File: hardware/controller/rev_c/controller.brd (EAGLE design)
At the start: 68.1 x 80 mm, 103 parts, among them J1 DM3AT-SF-PEJM5, J10 SOLDERJUMPERTRACE, J11 SOLDERJUMPERTRACE, J12 SOLDERJUMPERTRACE, J14 TC2030-JLINK-L, J15 TC2030-JLINK-L, J16 U.FL-R-SMT, J2 MICRO_USB_B_HIROSE_ZX62R-B-5P, J3 MICRO_USB_B_HIROSE_ZX62R-B-5P, J4 MODULE_CONTROLLER, J9 SOLDERJUMPERTRACE, Q1 DMN32D2LDF, SW1 B3U-1000P, SW2 PTS810SJ, SW3 SIP3240X, SW4 SIP3240X, SW5 SIP3240X, U1 FM25CLXXB-DG, U2 FTDI234XD, U3 RXM-GPS-RM-T, U4 SAM4LC8BA, U5 SAM4LC8BA, U6 SN74LVC1G125DBVR, U7 TS3USB30E, U8 TXS0108EVQFN20, X1 16MHz, X2 16MHz

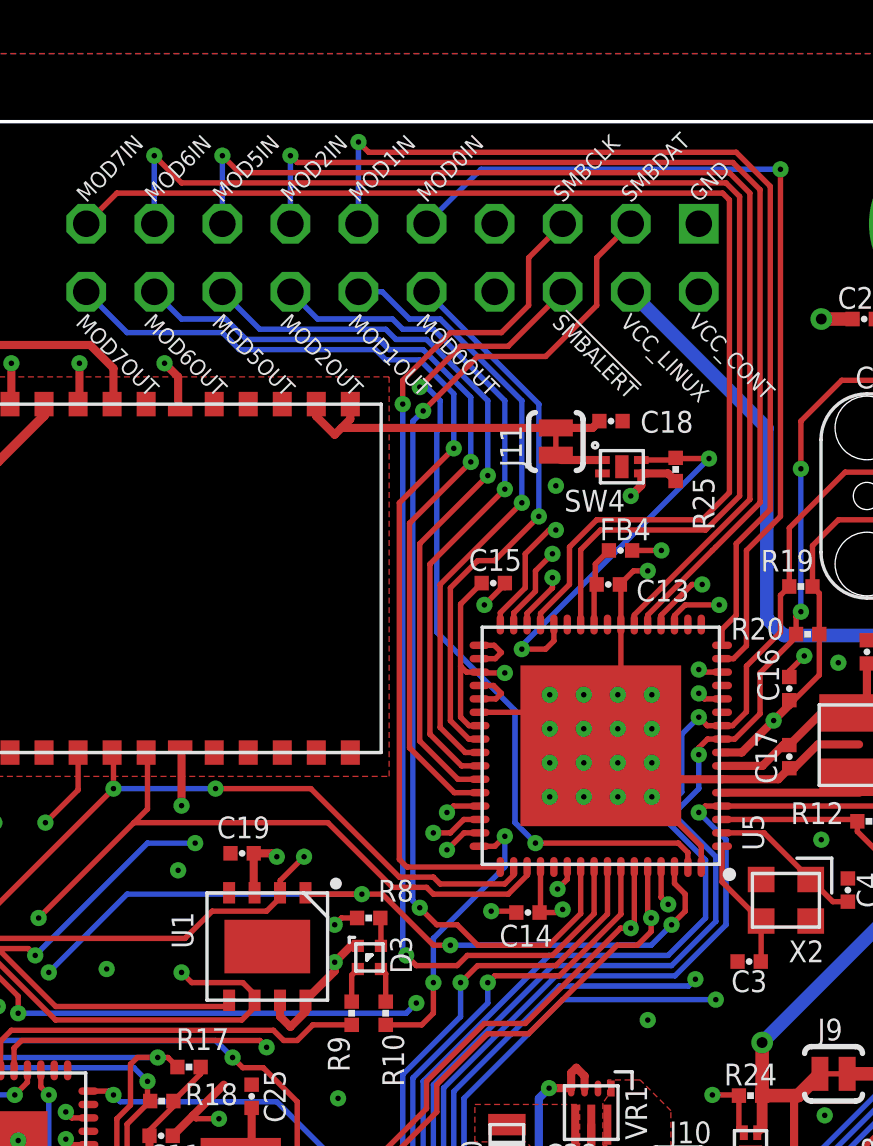
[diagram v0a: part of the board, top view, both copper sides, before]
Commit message: Added watchdog pin
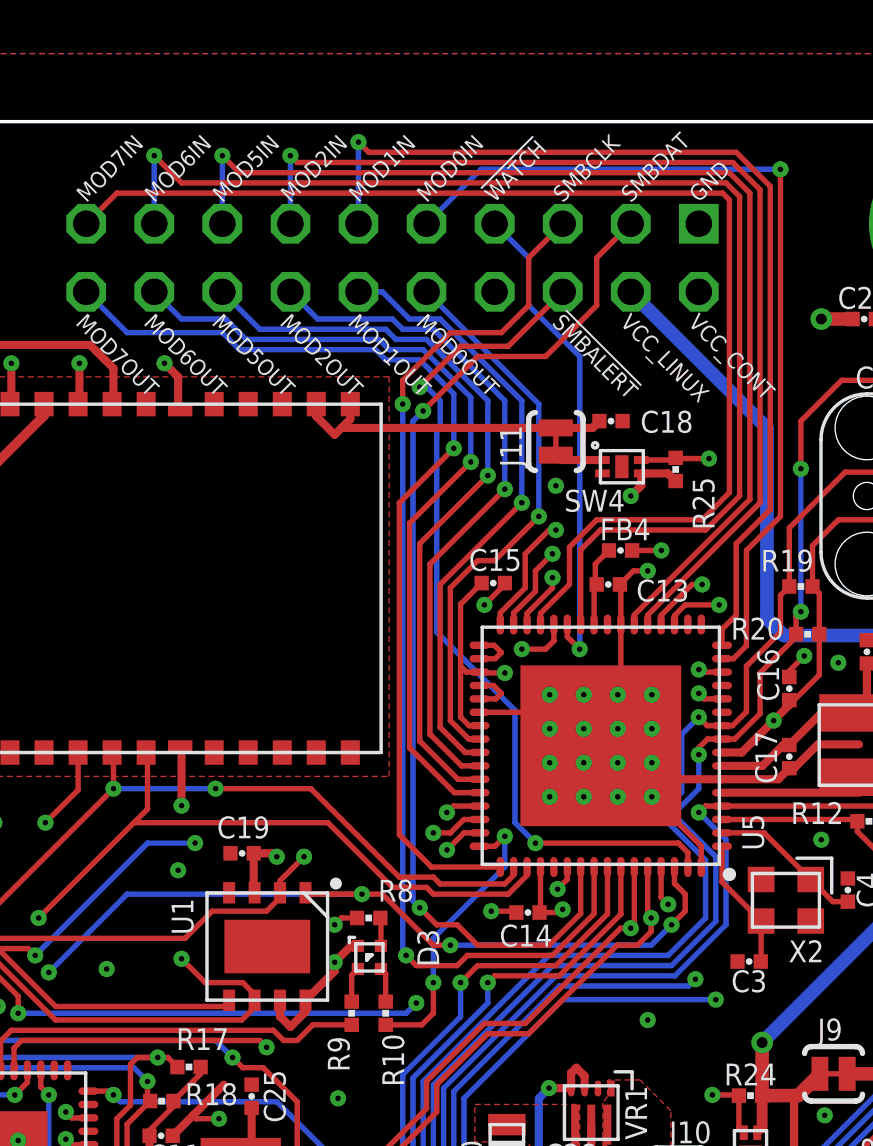
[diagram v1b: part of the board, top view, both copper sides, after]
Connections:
- new net !WATCHDOG: J4.7, U5.27
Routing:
- net !WATCHDOG: track 0.00 -> 18.3 mm, vias 0 -> 1
- net GPS_ENABLE_POWER: track 14.5 -> 15.3 mm
- net MOD7_OUT: track 37.4 -> 36.9 mm
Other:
- board text added: "!WATCH"
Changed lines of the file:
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@@
 <layer number="20" name="Dimension" color="15" fill="1" visible="yes" active="yes"/>
 <layer number="21" name="tPlace" color="7" fill="1" visible="yes" active="yes"/>
-<layer number="22" name="bPlace" color="7" fill="1" visible="yes" active="yes"/>
+<layer number="22" name="bPlace" color="7" fill="1" visible="no" active="yes"/>
 <layer number="23" name="tOrigins" color="15" fill="1" visible="yes" active="yes"/>
-<layer number="24" name="bOrigins" color="15" fill="1" visible="yes" active="yes"/>
+<layer number="24" name="bOrigins" color="15" fill="1" visible="no" active="yes"/>
 <layer number="25" name="tNames" color="7" fill="1" visible="yes" active="yes"/>
-<layer number="26" name="bNames" color="7" fill="1" visible="yes" active="yes"/>
+<layer number="26" name="bNames" color="7" fill="1" visible="no" active="yes"/>
 <layer number="27" name="tValues" color="7" fill="1" visible="no" active="yes"/>
 <layer number="28" name="bValues" color="7" fill="1" visible="no" active="yes"/>
@@
 <text x="27.686" y="-8.382" size="0.6096" layer="21" font="vector" ratio="12" rot="SR90" align="center">Edison
 Program</text>
+<text x="3.81" y="29.972" size="0.6096" layer="21" font="vector" ratio="12" rot="R45">!WATCH</text>
 </plain>
 <attributes>
@@
 <element name="U1" library="chips" package="TDFN-8" value="FM25CLXXB-DG" x="-4.6736" y="2.2352" smashed="yes" rot="R180">
 <attribute name="DIGIKEY" value="FM25CL64B-DGRA-ND" x="-4.6736" y="2.2352" size="1.778" layer="27" rot="R180" display="off"/>
-<attribute name="NAME" x="-8.2442" y="2.8448" size="0.8128" layer="25" font="vector" ratio="12" rot="R270" align="bottom-center"/>
+<attribute name="NAME" x="-8.2442" y="3.3528" size="0.8128" layer="25" font="vector" ratio="12" rot="R270" align="bottom-center"/>
 <attribute name="VALUE" x="-8.0736" y="2.2352" size="1.016" layer="27" font="vector" ratio="12" rot="R270" align="bottom-center"/>
 </element>
@@
 <element name="D3" library="leds" package="1MM_SQ_4PAD" value="SML-LX0404SIUPGUSB" x="-0.8636" y="1.8288" smashed="yes" rot="R90">
 <attribute name="DIGIKEY" value="67-2125-1-ND" x="-0.8636" y="-3.2512" size="1.778" layer="27" rot="R90" display="off"/>
-<attribute name="NAME" x="0.7256" y="1.9304" size="0.8128" layer="25" font="vector" ratio="12" rot="R90" align="bottom-center"/>
+<attribute name="NAME" x="1.7416" y="2.1844" size="0.8128" layer="25" font="vector" ratio="12" rot="R90" align="bottom-center"/>
 <attribute name="VALUE" x="0.9364" y="1.8288" size="1.016" layer="27" font="vector" ratio="12" rot="R90" align="bottom-center"/>
 </element>
@@
 <contactref element="J4" pad="20"/>
 <contactref element="U5" pad="49"/>
-<wire x1="4.0224" y1="5.2032" x2="0.5397" y2="5.2032" width="0.2032" layer="1"/>
-<wire x1="0.5397" y1="5.2032" x2="0.254" y2="5.4889" width="0.2032" layer="1"/>
-<wire x1="0.254" y1="5.4889" x2="0.254" y2="18.796" width="0.2032" layer="1"/>
+<wire x1="4.0224" y1="5.2032" x2="1.45413125" y2="5.2032" width="0.2032" layer="1"/>
+<wire x1="1.45413125" y1="5.2032" x2="0.254" y2="6.40333125" width="0.2032" layer="1"/>
+<wire x1="0.254" y1="6.40333125" x2="0.254" y2="18.796" width="0.2032" layer="1"/>
 <via x="2.286" y="20.828" extent="1-16" drill="0.2032"/>
 <wire x1="-0.635" y1="24.511" x2="-5.715" y2="24.511" width="0.2032" layer="16"/>
@@
 </signal>
 <signal name="VCC_CONTROLLER">
-<contactref element="J4" pad="2"/>
 <contactref element="J14" pad="1"/>
 <contactref element="C11" pad="1"/>
@@
 <wire x1="18.21306875" y1="6.80593125" x2="18.2651375" y2="6.858" width="0.2032" layer="1"/>
 <wire x1="18.2651375" y1="6.858" x2="19.05" y2="6.858" width="0.2032" layer="1"/>
+<contactref element="J4" pad="2"/>
 </signal>
 <signal name="VCC_LINUX_1V8">
@@
 <wire x1="5.969" y1="15.621" x2="5.969" y2="16.002" width="0.2032" layer="1"/>
 <via x="5.969" y="16.002" extent="1-16" drill="0.2032"/>
-<via x="-7.874" y="1.27" extent="1-16" drill="0.2032"/>
-<wire x1="-7.874" y1="1.27" x2="-7.493" y2="0.889" width="0.2032" layer="1"/>
-<wire x1="-7.493" y1="0.889" x2="-5.588" y2="0.889" width="0.2032" layer="1"/>
+<via x="-7.874" y="1.778" extent="1-16" drill="0.2032"/>
 <wire x1="-5.588" y1="0.889" x2="-5.1486" y2="0.4496" width="0.2032" layer="1"/>
 <wire x1="-5.1486" y1="0.4496" x2="-5.1486" y2="0.2286" width="0.2032" layer="1"/>
@@
 <wire x1="5.969" y1="16.002" x2="2.413" y2="16.002" width="0.2032" layer="15"/>
 <wire x1="2.413" y1="16.002" x2="1.016" y2="14.605" width="0.2032" layer="15"/>
-<wire x1="-4.191" y1="4.953" x2="-2.317596875" y2="4.953" width="0.2032" layer="15"/>
+<wire x1="-4.699" y1="4.953" x2="-2.317596875" y2="4.953" width="0.2032" layer="15"/>
 <wire x1="-2.317596875" y1="4.953" x2="1.016" y2="8.286596875" width="0.2032" layer="15"/>
 <wire x1="1.016" y1="8.286596875" x2="1.016" y2="14.605" width="0.2032" layer="15"/>
-<wire x1="-7.874" y1="1.27" x2="-4.191" y2="4.953" width="0.2032" layer="15"/>
+<wire x1="-5.588" y1="0.889" x2="-6.985" y2="0.889" width="0.2032" layer="1"/>
+<wire x1="-6.985" y1="0.889" x2="-7.874" y2="1.778" width="0.2032" layer="1"/>
+<wire x1="-4.699" y1="4.953" x2="-7.874" y2="1.778" width="0.2032" layer="15"/>
 </signal>
 <signal name="N$8">
@@
 <contactref element="U5" pad="28"/>
 <via x="4.826" y="13.335" extent="1-16" drill="0.2032"/>
-<wire x1="4.826" y1="13.462" x2="11.811" y2="20.447" width="0.2032" layer="16"/>
 <via x="11.811" y="20.447" extent="1-16" drill="0.2032"/>
 <wire x1="11.811" y1="20.447" x2="10.59306875" y2="20.447" width="0.2032" layer="1"/>
@@
 <wire x1="6.0224" y1="13.6424" x2="5.715" y2="13.335" width="0.2032" layer="1"/>
 <wire x1="5.715" y1="13.335" x2="4.826" y2="13.335" width="0.2032" layer="1"/>
-<wire x1="4.826" y1="13.462" x2="4.826" y2="13.335" width="0.2032" layer="16"/>
+<wire x1="4.826" y1="13.335" x2="6.985" y2="15.494" width="0.2032" layer="15"/>
+<wire x1="6.985" y1="15.494" x2="6.985" y2="17.018" width="0.2032" layer="15"/>
+<wire x1="6.985" y1="17.018" x2="7.747" y2="17.78" width="0.2032" layer="15"/>
+<wire x1="7.747" y1="17.78" x2="9.144" y2="17.78" width="0.2032" layer="15"/>
+<wire x1="9.144" y1="17.78" x2="11.811" y2="20.447" width="0.2032" layer="15"/>
 </signal>
 <signal name="N$56">
@@
 <wire x1="-27.94" y1="-1.905" x2="-28.956" y2="-0.889" width="0.2032" layer="15"/>
 <wire x1="-28.956" y1="-0.889" x2="-29.94533125" y2="0.10033125" width="0.2032" layer="1"/>
-<wire x1="-25.781" y1="-1.905" x2="-24.003" y2="-3.683" width="0.2032" layer="15"/>
-<wire x1="-24.003" y1="-3.683" x2="-24.003" y2="-9.652" width="0.2032" layer="15"/>
+<wire x1="-24.003" y1="-4.953" x2="-24.003" y2="-9.652" width="0.2032" layer="15"/>
 <wire x1="-24.003" y1="-9.652" x2="-21.336" y2="-12.319" width="0.2032" layer="15"/>
 <wire x1="-21.336" y1="-12.319" x2="-17.018" y2="-12.319" width="0.2032" layer="15"/>
@@
 <wire x1="-17.018" y1="-12.319" x2="-16.625" y2="-11.926" width="0.2032" layer="1"/>
 <wire x1="-16.625" y1="-11.926" x2="-16.625" y2="-11.4338" width="0.2032" layer="1"/>
+<wire x1="-24.003" y1="-4.953" x2="-24.638" y2="-4.318" width="0.2032" layer="15"/>
+<wire x1="-24.638" y1="-4.318" x2="-24.638" y2="-3.048" width="0.2032" layer="15"/>
+<wire x1="-24.638" y1="-3.048" x2="-25.781" y2="-1.905" width="0.2032" layer="15"/>
 </signal>
 <signal name="N$17">
@@
 <wire x1="2.032" y1="5.842" x2="-0.381" y2="5.842" width="0.2032" layer="15"/>
 </signal>
+<signal name="!WATCHDOG">
+<contactref element="J4" pad="7"/>
+<contactref element="U5" pad="27"/>
+<wire x1="6.5224" y1="14.2532" x2="6.5224" y2="13.7976" width="0.2032" layer="1"/>
+<wire x1="6.5224" y1="13.7976" x2="6.985" y2="13.335" width="0.2032" layer="1"/>
+<via x="6.985" y="13.335" extent="1-16" drill="0.2032"/>
+<wire x1="6.985" y1="13.335" x2="6.985" y2="24.257" width="0.2032" layer="16"/>
+<wire x1="6.985" y1="24.257" x2="5.08" y2="26.162" width="0.2032" layer="16"/>
+<wire x1="5.08" y1="26.162" x2="5.08" y2="27.94" width="0.2032" layer="16"/>
+<wire x1="5.08" y1="27.94" x2="3.81" y2="29.21" width="0.2032" layer="16"/>
+</signal>
 </signals>

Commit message: Controller rev C updates
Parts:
- removed R24: 1MΩ, passives:0402_RES
- removed R6: 1kΩ, passives:0402_RES
- added R29: 1MΩ, passives:0402_RES
- added SW6, SW7: B3U-1000P, switches:B3U-1000P
- added U33, U9: NCP301LSN30, signpost:SOT23-5
- SW2: value PTS810SJ -> B3U-1000P; device switches:PTS810SJ -> switches:B3U-1000P
- moved SW2 26.4 mm to (8.89, -0.76), turned to 180 degrees
- moved C14 1.52 mm to (3.53, 3.51)
- moved R7 0.99 mm to (-13.1, -20.2), turned to 180 degrees
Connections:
- net EDISON_LED2 renamed EDISON_INTERRUPT_1V8
- removed net N$12: R7.2, U8.12
- removed net N$37: D2.4, R6.1
- new net !ENABLE_LINUX: Q1.G1, U4.21
- new net EDISON_INTERRUPT: U4.57, U8.12
- new net STORAGE_INTERRUPT: U4.26, U5.53
- net !BACKPLANE_RESET: now also SW6.1; no longer SW2.1, SW2.2
- net !CONTROLLER_RESET: now also SW2.1, U33.1
- net !STORAGE_RESET: now also SW7.1, U9.1
- net GND: now also SW2.2, SW6.2, SW7.2, U33.3, U9.3; no longer SW2.3, SW2.4
- net LINUX_ENABLE_POWER: now also Q1.D1, R29.1; no longer R24.1, U4.21
- net N$50: now also R7.2; no longer R6.2
- net VCC_CONTROLLER: now also U33.2, U9.2
- net VCC_LINUX: now also R29.2; no longer R24.2
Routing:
- net !ENABLE_LINUX: track 0.00 -> 43.2 mm, vias 0 -> 2
- net STORAGE_INTERRUPT: track 0.00 -> 30.1 mm, vias 0 -> 3
- net LINUX_ENABLE_POWER: track 30.3 -> 13.8 mm
- net EDISON_INTERRUPT: track 0.00 -> 13.9 mm, vias 0 -> 2
- net !CONTROLLER_RESET: track 145.8 -> 154.6 mm, vias 3 -> 4
- net VCC_CONTROLLER: track 94.6 -> 100.0 mm, vias 18 -> 20
- net !BACKPLANE_RESET: track 43.5 -> 40.8 mm
- net N$12: track 2.59 -> 0.00 mm
- net N$37: track 1.11 -> 0.00 mm
- net !STORAGE_CS: track 80.6 -> 79.7 mm
- net MODULES_SDA: track 95.3 -> 94.6 mm, vias 4 -> 3
- net GPS_OUT_TX: track 92.6 -> 93.2 mm
- net MODULES_SCL: track 91.7 -> 91.2 mm, vias 3 -> 4
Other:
- board text added: "Controller JTAG"
- board text added: "Controller Reset"
- board text added: "Signpost Controller Branden Ghena 5/10/2017"
- board text added: "Storage Master JTAG"
- board text added: "Storage Master Reset"
- board text removed: "Signpost Controller Branden Ghena 3/10/2017"
